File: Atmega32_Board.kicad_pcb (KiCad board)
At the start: 2 copper layers, 75.6 x 57.8 mm, 26 parts, among them J1 POWER, J2 UART, J3 PORTD, J4 PORTC, J5 PORTB, U1 ATmega328P-P, Y1 Crystal

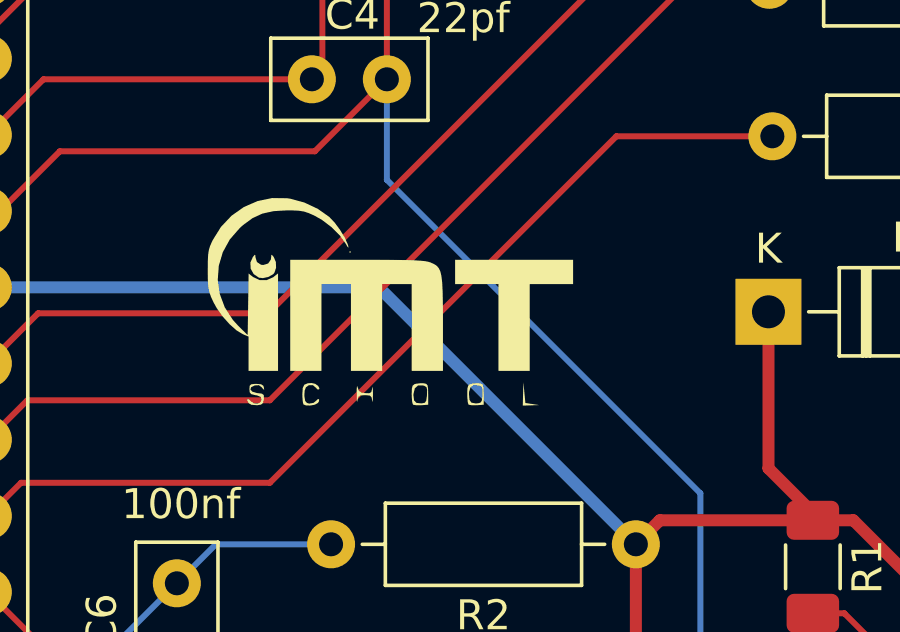
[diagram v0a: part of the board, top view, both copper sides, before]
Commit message: Added new Logo
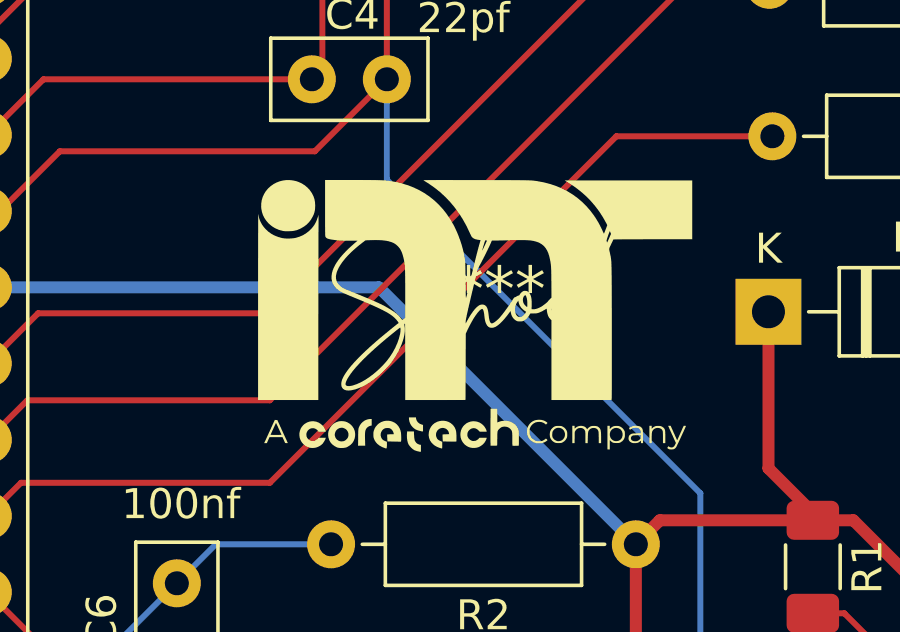
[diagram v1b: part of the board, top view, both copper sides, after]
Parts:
- removed the G*** at (134.9, 63.5)
- added G***: LOGO, logo_Footprints:imt_new3, F.Cu at (137.9, 63.1)

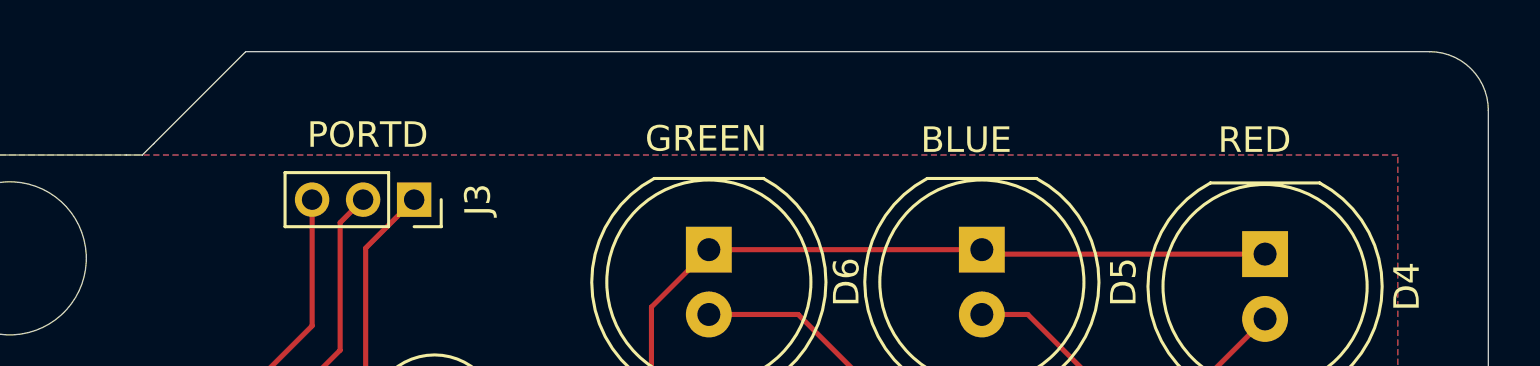
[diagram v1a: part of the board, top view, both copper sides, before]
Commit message: changed board size
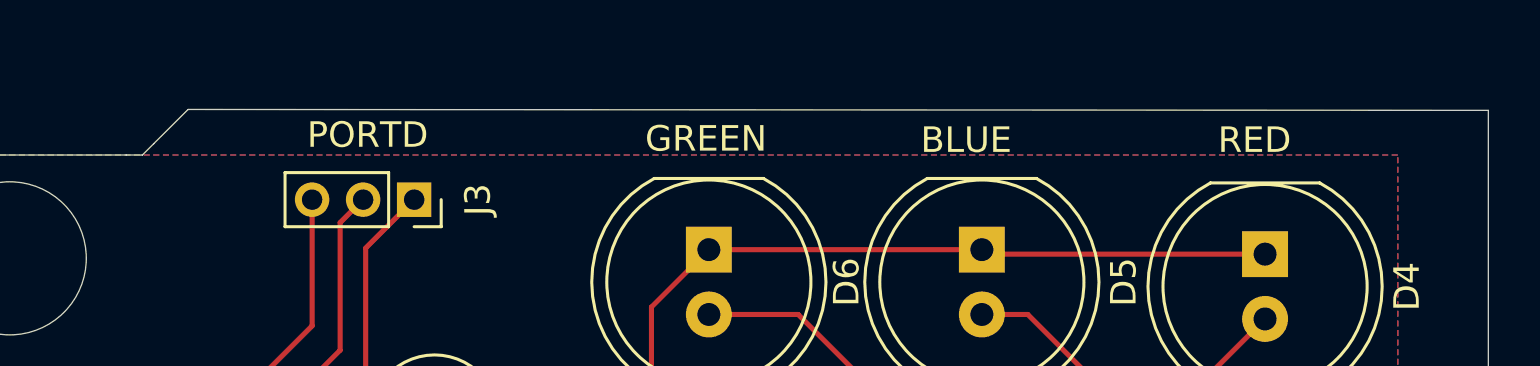
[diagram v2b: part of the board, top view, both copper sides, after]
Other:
- board size 75.6 x 57.8 mm -> 75.6 x 55.6 mm
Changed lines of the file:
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@@
-		(layer "Edge.Cuts")
-	)
-	(gr_arc
-		(start 172.75 29.7)
-		(mid 174.376346 30.373654)
-		(end 175.05 32)
-		(stroke
-			(width 0.05)
-			(type default)
-		)
 		(layer "Edge.Cuts")
 	)
@@
 	)
 	(gr_line
-		(start 126.35 29.7)
-		(end 172.75 29.7)
-		(stroke
-			(width 0.05)
-			(type default)
-		)
-		(layer "Edge.Cuts")
-	)
-	(gr_line
 		(start 163.304241 82.545759)
 		(end 158.3 87.55)
@@
 	)
 	(gr_line
+		(start 124.09 31.965)
+		(end 175.05 32)
+		(stroke
+			(width 0.05)
+			(type default)
+		)
+		(layer "Edge.Cuts")
+	)
+	(gr_line
 		(start 174.979302 77.155072)
 		(end 175.05 77.084374)
@@
 		(mid 100.035786 38.185786)
 		(end 101.45 37.6)
-		(stroke
-			(width 0.05)
-			(type default)
-		)
-		(layer "Edge.Cuts")
-	)
-	(gr_line
-		(start 126.35 29.7)
-		(end 122.743001 33.306999)
 		(stroke
 			(width 0.05)
@@
 		(stroke
 			(width 0.05)
+			(type default)
+		)
+		(layer "Edge.Cuts")
+	)
+	(gr_line
+		(start 122.743001 33.306999)
+		(end 124.09 31.965)
+		(stroke
+			(width 0.05)
